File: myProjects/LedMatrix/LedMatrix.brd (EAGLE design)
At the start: 50.5 x 50.8 mm, 8 parts, among them IC1 74HC595N, IC2 74HC595N, IC3 74HC595N

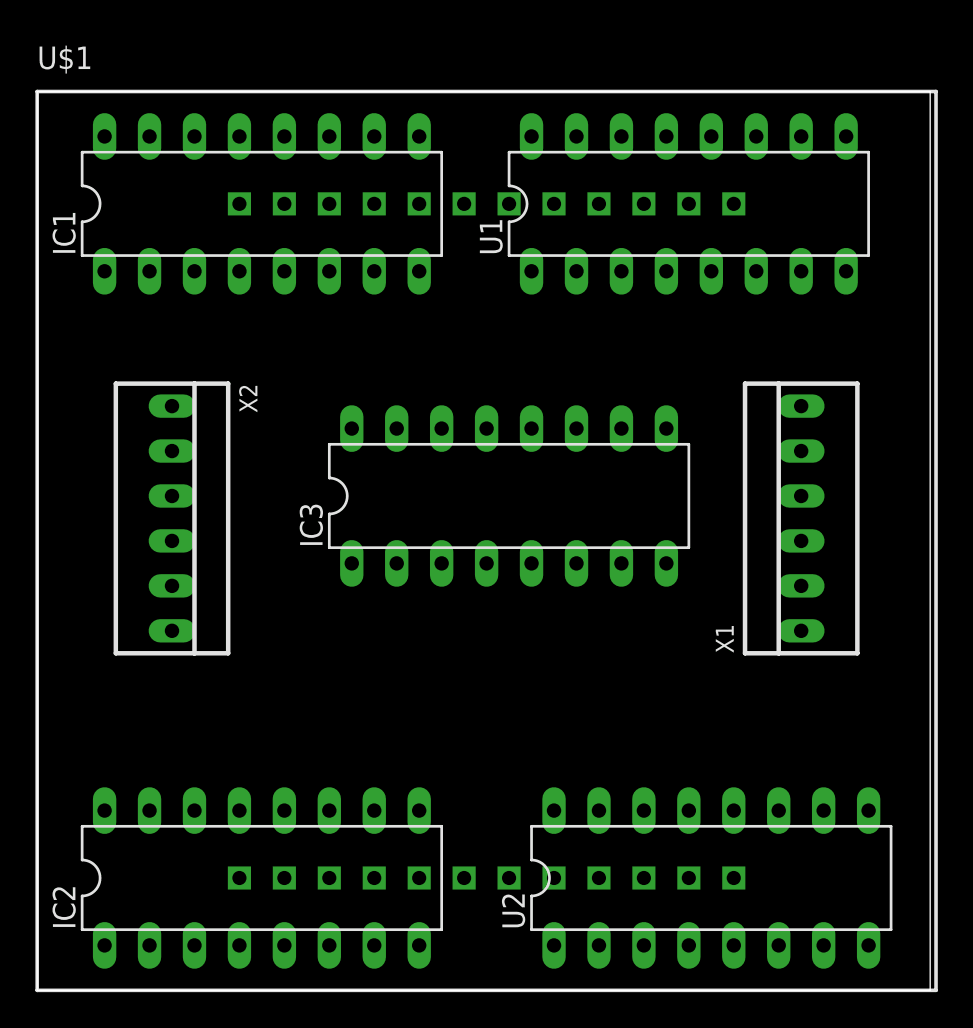
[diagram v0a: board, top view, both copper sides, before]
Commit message: completed board for led matrix
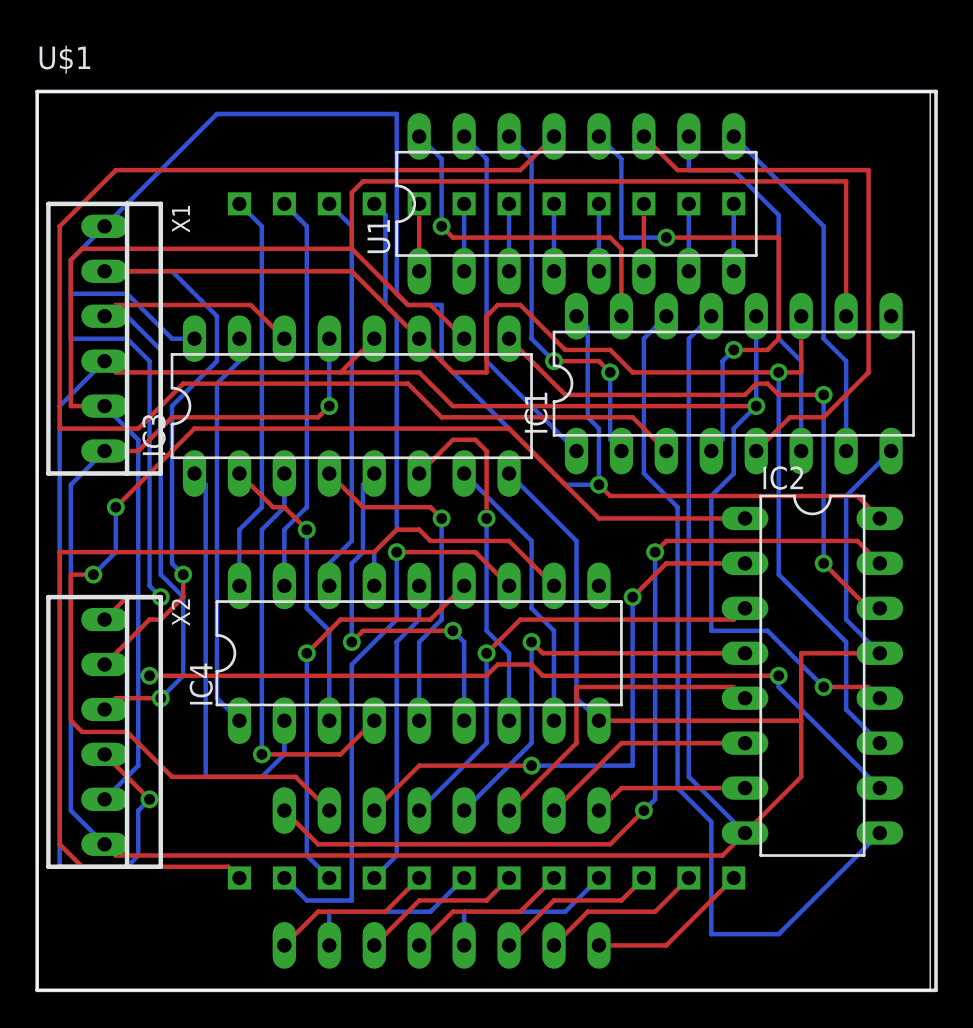
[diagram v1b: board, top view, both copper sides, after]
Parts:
- added IC4: ULN2803, uln-udn:DIL18
- U1, U2: value (none) -> RNET
- X1: value (none) -> INPUT
- X2: value (none) -> OUTPUT
- moved X1 40.7 mm to (3.81, 36.8), turned to 270 degrees
- moved IC2 33.1 mm to (43.8, 17.8), turned to 270 degrees
- moved IC1 28.5 mm to (39.4, 34.3)
- moved U2 15.2 mm to (22.9, 6.35), flipped to the bottom
- moved X2 12.7 mm to (3.81, 14.6)
- moved IC3 10.2 mm to (17.8, 33.0)
- moved U1 6.35 mm to (30.5, 44.5)
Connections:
- new net CLEAR: IC1.10, IC2.10, IC3.10, X1.5, X2.5
- new net CLK: IC1.11, IC2.11, IC3.11, X1.2, X2.2
- new net LATCH: IC1.12, IC2.12, IC3.12, X1.4, X2.4
- new net MOSI: IC3.14, X1.3, X2.3
- new net N$1: IC1.1, U1.15
- new net N$10: U$1.6, U1.2
- new net N$11: U$1.7, U1.3
- new net N$12: U$1.8, U1.4
- new net N$13: U$1.9, U1.5
- new net N$14: U$1.10, U1.6
- new net N$15: U$1.11, U1.7
- new net N$16: U$1.12, U1.8
- new net N$17: U$1.13, U2.1
- new net N$18: U$1.14, U2.2
- new net N$19: U$1.15, U2.3
- new net N$2: IC1.2, U1.14
- new net N$20: U$1.16, U2.4
- new net N$21: U$1.17, U2.5
- new net N$22: U$1.18, U2.6
- new net N$23: U$1.19, U2.7
- new net N$24: U$1.20, U2.8
- new net N$25: IC2.1, U2.10
- new net N$26: IC2.2, U2.11
- new net N$27: IC2.3, U2.12
- new net N$28: IC2.4, U2.13
- new net N$29: IC2.5, U2.14
- new net N$3: IC1.3, U1.13
- new net N$30: IC2.6, U2.15
- new net N$31: IC2.7, U2.16
- new net N$32: IC2.15, U2.9
- new net N$33: IC3.1, IC4.2
- new net N$34: IC3.2, IC4.3
- new net N$35: IC3.3, IC4.4
- new net N$36: IC3.4, IC4.5
- new net N$37: IC3.5, IC4.6
- new net N$38: IC3.6, IC4.7
- new net N$39: IC3.7, IC4.8
- new net N$4: IC1.4, U1.12
- new net N$40: IC3.15, IC4.1
- new net N$41: IC4.18, U$1.1
- new net N$42: IC4.17, U$1.2
- new net N$43: IC4.16, U$1.3
- new net N$44: IC4.15, U$1.4
- new net N$45: IC4.14, U$1.21
- new net N$46: IC4.13, U$1.22
- new net N$47: IC4.12, U$1.23
- new net N$48: IC4.11, U$1.24
- new net N$49: IC2.14, IC3.9
- new net N$5: IC1.5, U1.11
- new net N$50: IC1.14, IC2.9
- new net N$6: IC1.6, U1.10
- new net N$7: IC1.7, U1.9
- new net N$8: IC1.15, U1.16
- new net N$9: U$1.5, U1.1
- net GND: now also IC1.13, IC2.13, IC3.13, IC4.9, X1.6, X2.6
- net VCC: now also X1.1, X2.1
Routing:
- net GND: track 0.00 -> 166.1 mm, vias 0 -> 1
- net CLEAR: track 0.00 -> 143.0 mm, vias 0 -> 2
- net LATCH: track 0.00 -> 111.9 mm, vias 0 -> 3
- net VCC: track 0.00 -> 111.2 mm, vias 0 -> 2
- net CLK: track 0.00 -> 103.9 mm, vias 0 -> 2
- net N$3: track 0.00 -> 78.4 mm
- net N$25: track 0.00 -> 70.1 mm, vias 0 -> 2
- net N$48: track 0.00 -> 57.2 mm
- net N$32: track 0.00 -> 50.3 mm, vias 0 -> 2
- net N$50: track 0.00 -> 48.9 mm
- net MOSI: track 0.00 -> 39.4 mm, vias 0 -> 1
- net N$49: track 0.00 -> 33.4 mm, vias 0 -> 2
- net N$5: track 0.00 -> 33.1 mm
- net N$26: track 0.00 -> 32.3 mm, vias 0 -> 2
- net N$47: track 0.00 -> 32.2 mm, vias 0 -> 1
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
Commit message: fixed some labelling
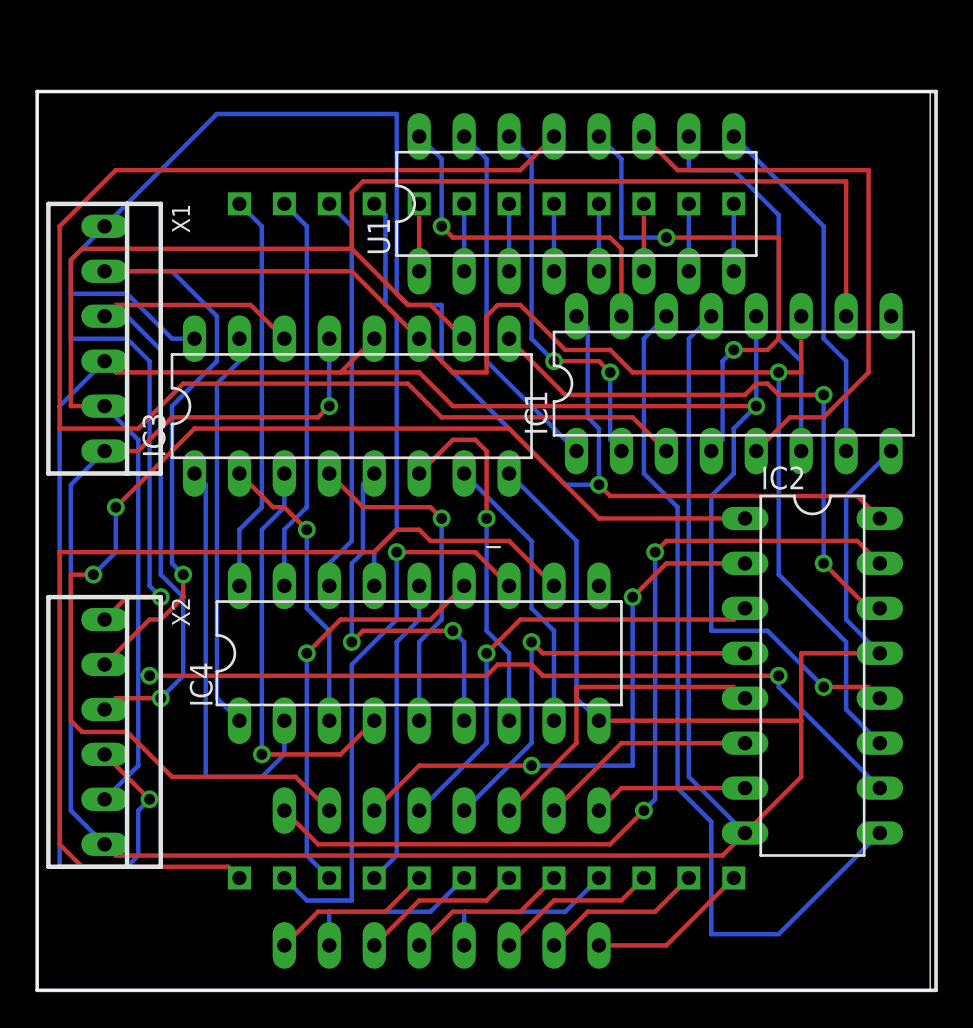
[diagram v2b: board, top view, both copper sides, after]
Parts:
- _: value WLG-M2088A/8EG -> (none)
- renumbered U$1 to _
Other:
- board text added: "11/03/15"
- board text added: "Sibosop"
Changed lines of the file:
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@@
 <wire x1="50.47" y1="50.79" x2="0" y2="50.79" width="0" layer="20"/>
 <wire x1="0" y1="50.79" x2="0" y2="0" width="0" layer="20"/>
+<text x="2.54" y="5.08" size="1.27" layer="26">Sibosop</text>
+<text x="2.54" y="2.54" size="1.016" layer="26">11/03/15</text>
 </plain>
 <attributes>
@@
 </autorouter>
 <elements>
-<element name="U$1" library="led-matrix-v2" package="WLG-M2088A/8EG" value="WLG-M2088A/8EG" x="25.4" y="25.4"/>
+<element name="_" library="led-matrix-v2" package="WLG-M2088A/8EG" value="" x="25.4" y="25.4" smashed="yes">
+<attribute name="NAME" x="25.4" y="25.4" size="1.27" layer="25"/>
+<attribute name="VALUE" x="25.4" y="25.4" size="1.27" layer="27"/>
+</element>
 <element name="IC1" library="74xx-eu" package="DIL16" value="74HC595N" x="39.37" y="34.29"/>
 <element name="IC2" library="74xx-eu" package="DIL16" value="74HC595N" x="43.815" y="17.78" rot="R270"/>
 <element name="IC3" library="74xx-eu" package="DIL16" value="74HC595N" x="17.78" y="33.02"/>
 <element name="U1" library="sibosop" package="DIP16" value="RNET" x="30.48" y="44.45"/>
-<element name="U2" library="sibosop" package="DIP16" value="RNET" x="22.86" y="6.35" rot="MR0"/>
-<element name="X1" library="sibosop-con-molex" package="22-23-2061" value="INPUT" x="3.81" y="36.83" rot="R270"/>
-<element name="X2" library="sibosop-con-molex" package="22-23-2061" value="OUTPUT" x="3.81" y="14.605" rot="R270"/>
+<element name="U2" library="sibosop" package="DIP16" value="RNET" x="22.86" y="6.35" smashed="yes" rot="MR0">
+<attribute name="NAME" x="33.401" y="3.429" size="1.27" layer="26" ratio="10" rot="MR90"/>
+<attribute name="VALUE" x="25.273" y="5.715" size="1.27" layer="27" ratio="10"/>
+</element>
+<element name="X1" library="sibosop-con-molex" package="22-23-2061" value="INPUT" x="3.81" y="36.83" smashed="yes" rot="R270">
+<attribute name="NAME" x="7.62" y="44.45" size="1.016" layer="25" ratio="14" rot="R270"/>
+<attribute name="VALUE" x="1.27" y="45.72" size="1.016" layer="27" ratio="14"/>
+</element>
+<element name="X2" library="sibosop-con-molex" package="22-23-2061" value="OUTPUT" x="3.81" y="14.605" smashed="yes" rot="R270">
+<attribute name="NAME" x="7.62" y="22.225" size="1.016" layer="25" ratio="14" rot="R270"/>
+<attribute name="VALUE" x="1.905" y="24.13" size="1.016" layer="27" ratio="14"/>
+</element>
 <element name="IC4" library="uln-udn" package="DIL18" value="ULN2803" x="21.59" y="19.05"/>
 </elements>
@@
 </signal>
 <signal name="N$9">
-<contactref element="U$1" pad="5"/>
+<contactref element="_" pad="5"/>
 <contactref element="U1" pad="1"/>
 <wire x1="21.59" y1="40.64" x2="21.59" y2="44.45" width="0.254" layer="1"/>
 </signal>
 <signal name="N$10">
-<contactref element="U$1" pad="6"/>
+<contactref element="_" pad="6"/>
 <contactref element="U1" pad="2"/>
 <wire x1="24.13" y1="40.64" x2="24.13" y2="44.45" width="0.254" layer="16"/>
 </signal>
 <signal name="N$11">
-<contactref element="U$1" pad="7"/>
+<contactref element="_" pad="7"/>
 <contactref element="U1" pad="3"/>
 <wire x1="26.67" y1="40.64" x2="26.67" y2="44.45" width="0.254" layer="16"/>
 </signal>
 <signal name="N$12">
-<contactref element="U$1" pad="8"/>
+<contactref element="_" pad="8"/>
 <contactref element="U1" pad="4"/>
 <wire x1="29.21" y1="40.64" x2="29.21" y2="44.45" width="0.254" layer="16"/>
 </signal>
 <signal name="N$13">
-<contactref element="U$1" pad="9"/>
+<contactref element="_" pad="9"/>
 <contactref element="U1" pad="5"/>
 <wire x1="31.75" y1="40.64" x2="31.75" y2="44.45" width="0.254" layer="16"/>
 </signal>
 <signal name="N$14">
-<contactref element="U$1" pad="10"/>
+<contactref element="_" pad="10"/>
 <contactref element="U1" pad="6"/>
 <wire x1="34.29" y1="40.64" x2="34.29" y2="44.45" width="0.254" layer="1"/>
 </signal>
 <signal name="N$15">
-<contactref element="U$1" pad="11"/>
+<contactref element="_" pad="11"/>
 <contactref element="U1" pad="7"/>
 <wire x1="36.83" y1="40.64" x2="36.83" y2="44.45" width="0.254" layer="16"/>
 </signal>
 <signal name="N$16">
-<contactref element="U$1" pad="12"/>
+<contactref element="_" pad="12"/>
 <contactref element="U1" pad="8"/>
 <wire x1="39.37" y1="40.64" x2="39.37" y2="44.45" width="0.254" layer="16"/>
 </signal>
 <signal name="N$17">
-<contactref element="U$1" pad="13"/>
+<contactref element="_" pad="13"/>
 <contactref element="U2" pad="1"/>
 <wire x1="35.56" y1="2.54" x2="39.37" y2="6.35" width="0.254" layer="1"/>
@@
 </signal>
 <signal name="N$18">
-<contactref element="U$1" pad="14"/>
+<contactref element="_" pad="14"/>
 <contactref element="U2" pad="2"/>
 <wire x1="34.925" y1="4.445" x2="36.83" y2="6.35" width="0.254" layer="1"/>
@@
 </signal>
 <signal name="N$19">
-<contactref element="U$1" pad="15"/>
+<contactref element="_" pad="15"/>
 <contactref element="U2" pad="3"/>
 <wire x1="33.02" y1="5.08" x2="34.29" y2="6.35" width="0.254" layer="1"/>
@@
 </signal>
 <signal name="N$20">
-<contactref element="U$1" pad="16"/>
+<contactref element="_" pad="16"/>
 <contactref element="U2" pad="4"/>
 <wire x1="29.845" y1="4.445" x2="31.75" y2="6.35" width="0.254" layer="16"/>
@@
 </signal>
 <signal name="N$21">
-<contactref element="U$1" pad="17"/>
+<contactref element="_" pad="17"/>
 <contactref element="U2" pad="5"/>
 <wire x1="27.305" y1="4.445" x2="29.21" y2="6.35" width="0.254" layer="1"/>
@@
 </signal>
 <signal name="N$22">
-<contactref element="U$1" pad="18"/>
+<contactref element="_" pad="18"/>
 <contactref element="U2" pad="6"/>
 <wire x1="25.4" y1="5.08" x2="26.67" y2="6.35" width="0.254" layer="1"/>
@@
 </signal>
 <signal name="N$23">
-<contactref element="U$1" pad="19"/>
+<contactref element="_" pad="19"/>
 <contactref element="U2" pad="7"/>
 <wire x1="22.225" y1="4.445" x2="24.13" y2="6.35" width="0.254" layer="16"/>
@@
 </signal>
 <signal name="N$24">
-<contactref element="U$1" pad="20"/>
+<contactref element="_" pad="20"/>
 <contactref element="U2" pad="8"/>
 <wire x1="19.685" y1="4.445" x2="21.59" y2="6.35" width="0.254" layer="1"/>
@@
 <signal name="N$41">
 <contactref element="IC4" pad="18"/>
-<contactref element="U$1" pad="1"/>
+<contactref element="_" pad="1"/>
 <wire x1="12.7" y1="43.18" x2="11.43" y2="44.45" width="0.254" layer="16"/>
 <wire x1="12.7" y1="27.305" x2="12.7" y2="43.18" width="0.254" layer="16"/>
@@
 <signal name="N$42">
 <contactref element="IC4" pad="17"/>
-<contactref element="U$1" pad="2"/>
+<contactref element="_" pad="2"/>
 <wire x1="15.24" y1="43.18" x2="13.97" y2="44.45" width="0.254" layer="16"/>
 <wire x1="15.24" y1="27.305" x2="15.24" y2="43.18" width="0.254" layer="16"/>
@@
 <signal name="N$43">
 <contactref element="IC4" pad="16"/>
-<contactref element="U$1" pad="3"/>
+<contactref element="_" pad="3"/>
 <wire x1="17.78" y1="43.18" x2="16.51" y2="44.45" width="0.254" layer="16"/>
 <wire x1="17.78" y1="25.4" x2="17.78" y2="43.18" width="0.254" layer="16"/>
@@
 <signal name="N$44">
 <contactref element="IC4" pad="15"/>
-<contactref element="U$1" pad="4"/>
+<contactref element="_" pad="4"/>
 <wire x1="19.685" y1="43.815" x2="19.05" y2="44.45" width="0.254" layer="16"/>
 <wire x1="19.685" y1="38.735" x2="19.685" y2="43.815" width="0.254" layer="16"/>
@@
 <signal name="N$45">
 <contactref element="IC4" pad="14"/>
-<contactref element="U$1" pad="21"/>
+<contactref element="_" pad="21"/>
 <wire x1="20.32" y1="7.62" x2="19.05" y2="6.35" width="0.254" layer="16"/>
 <wire x1="20.32" y1="19.685" x2="20.32" y2="7.62" width="0.254" layer="16"/>
@@
 <signal name="N$46">
 <contactref element="IC4" pad="13"/>
-<contactref element="U$1" pad="22"/>
+<contactref element="_" pad="22"/>
 <wire x1="15.24" y1="7.62" x2="16.51" y2="6.35" width="0.254" layer="16"/>
 <wire x1="15.24" y1="19.05" x2="15.24" y2="7.62" width="0.254" layer="16"/>
@@
 <signal name="N$47">
 <contactref element="IC4" pad="12"/>
-<contactref element="U$1" pad="23"/>
+<contactref element="_" pad="23"/>
 <wire x1="15.24" y1="5.08" x2="13.97" y2="6.35" width="0.254" layer="16"/>
 <wire x1="17.78" y1="5.08" x2="15.24" y2="5.08" width="0.254" layer="16"/>
@@
 <signal name="N$48">
 <contactref element="IC4" pad="11"/>
-<contactref element="U$1" pad="24"/>
+<contactref element="_" pad="24"/>
 <wire x1="10.795" y1="6.985" x2="11.43" y2="6.35" width="0.254" layer="1"/>
 <wire x1="2.54" y1="6.985" x2="10.795" y2="6.985" width="0.254" layer="1"/>
